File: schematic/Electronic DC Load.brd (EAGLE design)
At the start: 100 x 51.2 mm, 104 parts, among them J1 POWER_JACKPTH_LOCK, J2 AVR_SPI_PROG_3X2PTH, J3 FAN, J4 KF762-2, Q1 16MHz, Q2 IRFP250NV, Q3 600mA/40V, U1 AMS1117-5.0, U10 AD8629ARZ, U2 REF5050_D_8, U3 ATMEGA328P_TQFP, U4 MP1584EN, U5 LM35_LP_3, U6 AD7190BRUZ, U7 AD5541ARZ, U8 INA210AIDCKRG4, U9 PCF8574_DW_16

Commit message: Change debouncing filter network resistor to 1K
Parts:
- R12, R17, R19, R22, R24, R25, R27: value 10K -> 1K
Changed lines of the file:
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@@
 <attribute name="VALUE" x="38.0238" y="40.0304" size="1.27" layer="27"/>
 </element>
-<element name="R12" library="resistor" library_urn="urn:adsk.eagle:library:348" package="R0603" package3d_urn="urn:adsk.eagle:package:26057/1" value="10K" x="94.9452" y="10.2108" smashed="yes" rot="MR270">
+<element name="R12" library="resistor" library_urn="urn:adsk.eagle:library:348" package="R0603" package3d_urn="urn:adsk.eagle:package:26057/1" value="1K" x="94.9452" y="10.2108" smashed="yes" rot="MR270">
 <attribute name="NAME" x="94.1832" y="12.5222" size="0.6096" layer="26" rot="MR180"/>
 <attribute name="VALUE" x="96.8502" y="10.8458" size="1.27" layer="28" rot="MR270"/>
@@
 <attribute name="VALUE" x="40.4368" y="7.8486" size="1.27" layer="28" rot="MR270"/>
 </element>
-<element name="R19" library="resistor" library_urn="urn:adsk.eagle:library:348" package="R0603" package3d_urn="urn:adsk.eagle:package:26057/1" value="10K" x="41.7068" y="8.9916" smashed="yes" rot="MR0">
+<element name="R19" library="resistor" library_urn="urn:adsk.eagle:library:348" package="R0603" package3d_urn="urn:adsk.eagle:package:26057/1" value="1K" x="41.7068" y="8.9916" smashed="yes" rot="MR0">
 <attribute name="NAME" x="41.7068" y="10.2108" size="0.6096" layer="26" rot="MR0"/>
 <attribute name="VALUE" x="42.3418" y="7.0866" size="1.27" layer="28" rot="MR0"/>
@@
 <attribute name="VALUE" x="50.8508" y="7.8486" size="1.27" layer="28" rot="MR270"/>
 </element>
-<element name="R17" library="resistor" library_urn="urn:adsk.eagle:library:348" package="R0603" package3d_urn="urn:adsk.eagle:package:26057/1" value="10K" x="51.9938" y="8.9916" smashed="yes" rot="MR0">
+<element name="R17" library="resistor" library_urn="urn:adsk.eagle:library:348" package="R0603" package3d_urn="urn:adsk.eagle:package:26057/1" value="1K" x="51.9938" y="8.9916" smashed="yes" rot="MR0">
 <attribute name="NAME" x="51.943" y="10.3124" size="0.6096" layer="26" rot="MR0"/>
 <attribute name="VALUE" x="52.6288" y="7.0866" size="1.27" layer="28" rot="MR0"/>
@@
 <attribute name="VALUE" x="85.1662" y="8.8138" size="1.27" layer="28" rot="MR180"/>
 </element>
-<element name="R22" library="resistor" library_urn="urn:adsk.eagle:library:348" package="R0603" package3d_urn="urn:adsk.eagle:package:26057/1" value="10K" x="85.8012" y="4.6228" smashed="yes" rot="MR180">
+<element name="R22" library="resistor" library_urn="urn:adsk.eagle:library:348" package="R0603" package3d_urn="urn:adsk.eagle:package:26057/1" value="1K" x="85.8012" y="4.6228" smashed="yes" rot="MR180">
 <attribute name="VALUE" x="85.1662" y="6.5278" size="1.27" layer="28" rot="MR180"/>
 </element>
@@
 <attribute name="VALUE" x="85.1662" y="11.3538" size="1.27" layer="28" rot="MR180"/>
 </element>
-<element name="R24" library="resistor" library_urn="urn:adsk.eagle:library:348" package="R0603" package3d_urn="urn:adsk.eagle:package:26057/1" value="10K" x="85.8012" y="11.7348" smashed="yes" rot="MR180">
+<element name="R24" library="resistor" library_urn="urn:adsk.eagle:library:348" package="R0603" package3d_urn="urn:adsk.eagle:package:26057/1" value="1K" x="85.8012" y="11.7348" smashed="yes" rot="MR180">
 <attribute name="VALUE" x="85.1662" y="13.6398" size="1.27" layer="28" rot="MR180"/>
 </element>
@@
 <attribute name="VALUE" x="61.0108" y="7.8486" size="1.27" layer="28" rot="MR270"/>
 </element>
-<element name="R27" library="resistor" library_urn="urn:adsk.eagle:library:348" package="R0603" package3d_urn="urn:adsk.eagle:package:26057/1" value="10K" x="62.2808" y="8.9916" smashed="yes" rot="MR0">
+<element name="R27" library="resistor" library_urn="urn:adsk.eagle:library:348" package="R0603" package3d_urn="urn:adsk.eagle:package:26057/1" value="1K" x="62.2808" y="8.9916" smashed="yes" rot="MR0">
 <attribute name="NAME" x="62.1284" y="10.16" size="0.6096" layer="26" rot="MR0"/>
 <attribute name="VALUE" x="62.9158" y="7.0866" size="1.27" layer="28" rot="MR0"/>
@@
 <attribute name="VALUE" x="71.3486" y="7.7978" size="1.27" layer="28" rot="MR270"/>
 </element>
-<element name="R25" library="resistor" library_urn="urn:adsk.eagle:library:348" package="R0603" package3d_urn="urn:adsk.eagle:package:26057/1" value="10K" x="72.5678" y="8.9916" smashed="yes" rot="MR0">
+<element name="R25" library="resistor" library_urn="urn:adsk.eagle:library:348" package="R0603" package3d_urn="urn:adsk.eagle:package:26057/1" value="1K" x="72.5678" y="8.9916" smashed="yes" rot="MR0">
 <attribute name="NAME" x="72.4408" y="10.16" size="0.6096" layer="26" rot="MR0"/>
 <attribute name="VALUE" x="73.2028" y="7.0866" size="1.27" layer="28" rot="MR0"/>

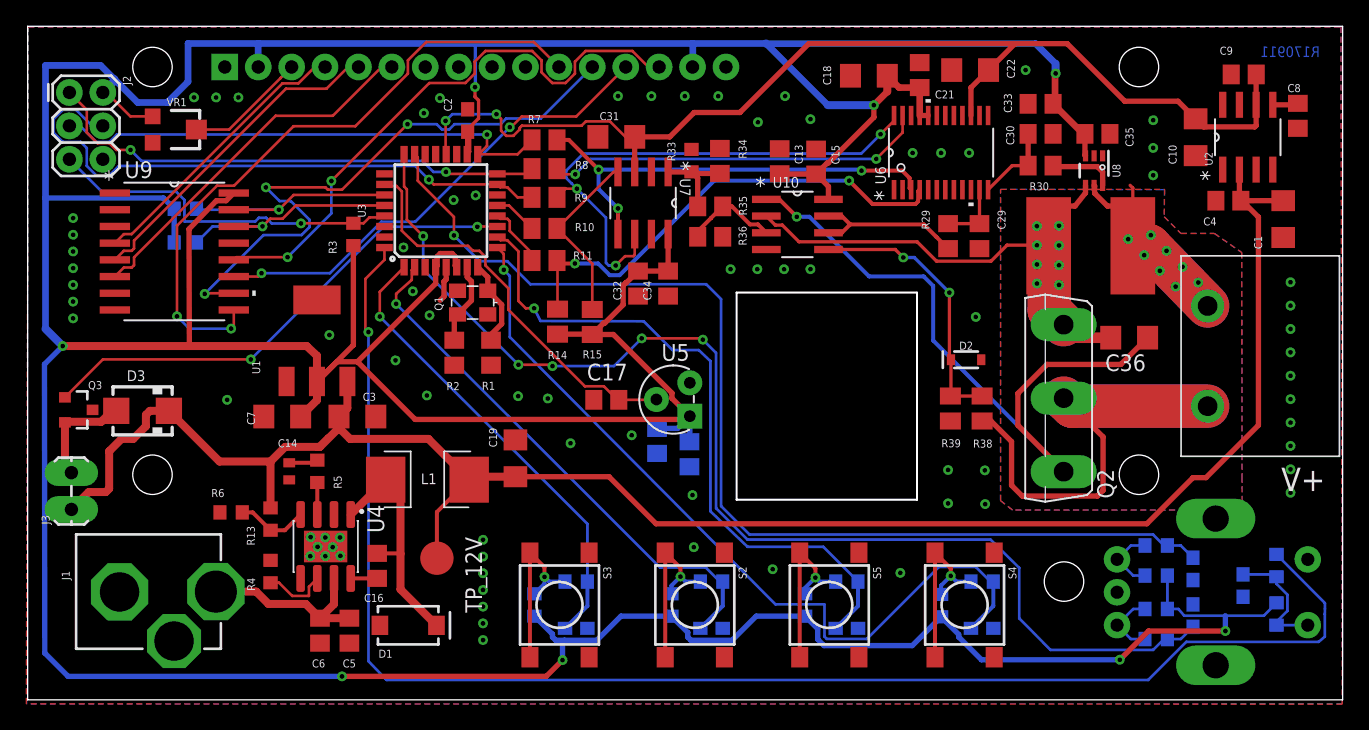
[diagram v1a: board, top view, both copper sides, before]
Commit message: Fix lableling errors
Fix a few errors in the labeling of resistors and capacitors
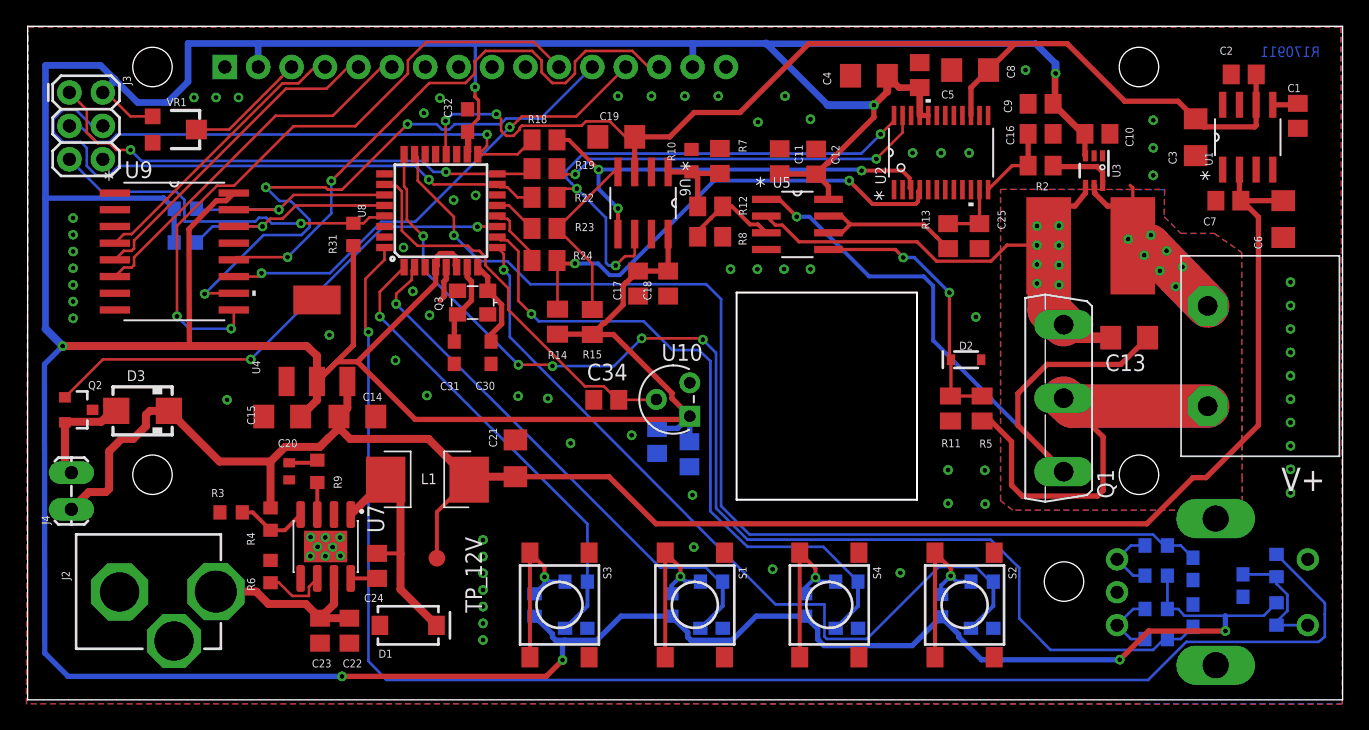
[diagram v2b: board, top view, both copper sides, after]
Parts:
- removed R38: 39K 0.1%, resistor:M0805
- removed R39: 1K 0.1%, resistor:M0805
- added C37: 1uF, resistor:C0805
- added C38: 100nF, resistor:C0805
- C1, C22: value 10uF -> 1uF; device resistor:C1206 -> resistor:C0805
- C10: value 47uF -> 100nF; device resistor:C1206 -> resistor:C0805
- C13, C8: value 1uF -> 10uF; device resistor:C0805 -> resistor:C1206
- C14: value 150pF -> 10uF; device resistor:C0402 -> resistor:C1206
- C15: value 100nF -> 22uF; device resistor:C0805 -> resistor:C1206
- C16, C34: value 100nF -> 1uF
- C18: value 10uF -> 100nF; device resistor:C1206 -> resistor:C0805
- C19: value 47uF -> 10uF
- C2, C25: value 100nF -> 1uF; device resistor:C0603 -> resistor:C0805
- C20: value 100nF -> 150pF; device resistor:C0603 -> resistor:C0402
- C21: value 100nF -> 47uF; device resistor:C0805 -> resistor:C1206
- C23, C24: device resistor:C0603 -> resistor:C0805
- C29, C32, C33: value 1uF -> 100nF; device resistor:C0805 -> resistor:C0603
- C3: value 10uF -> 47uF
- C30: value 1uF -> 8.2pF; device resistor:C0805 -> resistor:C0603
- C31: value 10uF -> 8.2pF; device resistor:C1206 -> resistor:C0603
- C35: device resistor:C0805 -> resistor:C0603
- C36: value 10uF -> 100nF; device resistor:C1206 -> resistor:C0603
- C4, C6: value 100nF -> 10uF; device resistor:C0805 -> resistor:C1206
- C5: value 1uF -> 100nF
- C7: value 22uF -> 100nF; device resistor:C1206 -> resistor:C0805
- J1: value POWER_JACKPTH_LOCK -> KF762-2; device SparkFun-Connectors:POWER_JACK_PTH_LOCK -> 0_discrete:KF762-2
- J2: value AVR_SPI_PROG_3X2PTH -> POWER_JACKPTH_LOCK; device SparkFun-Connectors:2X3 -> SparkFun-Connectors:POWER_JACK_PTH_LOCK
- J3: value FAN -> AVR_SPI_PROG_3X2PTH; device SparkFun-Connectors:1X02_LOCK_LONGPADS -> SparkFun-Connectors:2X3
- J4: value KF762-2 -> FAN; device 0_discrete:KF762-2 -> SparkFun-Connectors:1X02_LOCK_LONGPADS
- Q1: value 16MHz -> IRFP250NV; device crystal-geyer_V1_0:3.2X2.5_KX-7 -> 0_discrete:TO247BV
- Q2: value IRFP250NV -> 600mA/40V; device 0_discrete:TO247BV -> SparkFun-DiscreteSemi:SOT23-3
- Q3: value 600mA/40V -> 16MHz; device SparkFun-DiscreteSemi:SOT23-3 -> crystal-geyer_V1_0:3.2X2.5_KX-7
- R1: value 10pF -> .005; device resistor:R0805 -> 0_sup:2728
- R10: value 100 -> 10K; device resistor:M0805 -> resistor:R0603
- R11: value 100 -> 1K 0.1%
- R12: value 1K -> 39K 0.1%; device resistor:R0603 -> resistor:R0805
- R13: value 150K -> 1K; device resistor:R0603 -> resistor:R0805
- R17, R25, R27: value 1K -> 10K
- R18, R23: value 10K -> 100; device resistor:R0603 -> resistor:M0805
- R19, R22, R24: value 1K -> 100; device resistor:R0603 -> resistor:M0805
- R2: value 10pF -> 1K
- R29, R30: value 1K -> 10K; device resistor:R0805 -> resistor:R0603
- R3: value 10K -> 10.5K
- R34: value 1uF -> 10K; device resistor:R0805 -> resistor:R0603
- R35: value 39K 0.1% -> 10K; device resistor:R0805 -> resistor:R0603
- R36: value 10K 0.1% -> 10K; device resistor:R0805 -> resistor:R0603
- R37: value .005 -> 10K; device 0_sup:2728 -> resistor:R0603
- R4: value 120K -> 150K
- R5: value 500K -> 9K9 0.1%; device resistor:R0603 -> resistor:M0805
- R6: value 10.5K -> 120K
- R7: value 100 -> 1uF; device resistor:M0805 -> resistor:R0805
- R8: value 100 -> 10K 0.1%; device resistor:M0805 -> resistor:R0805
- R9: value 100 -> 510K; device resistor:M0805 -> resistor:R0603
- S1: value ENCODER_SWITCH_EC11 -> SWITCH_6X6; device 0_discrete:ROTARY_ENCODER_EC11 -> 0_discrete:SWITCH_SMD_6MM
- S5: value SWITCH_6X6 -> ENCODER_SWITCH_EC11; device 0_discrete:SWITCH_SMD_6MM -> 0_discrete:ROTARY_ENCODER_EC11
- TP_12V: value TPB2,54 -> TPB1,27; device testpad:B2,54 -> testpad:B1,27
- U1: value AMS1117-5.0 -> REF5050_D_8; device AMS1117-5.0:SOT223 -> 0_texas-instrument:D8
- U10: value AD8629ARZ -> LM35_LP_3; device 0_analog-devices:R_8 -> 0_texas-instrument:Z03A
- U2: value REF5050_D_8 -> AD7190BRUZ; device 0_texas-instrument:D8 -> 0_analog-devices:RU_24
- U3: value ATMEGA328P_TQFP -> INA210AIDCKRG4; device SparkFun-IC-Microcontroller:TQFP32-08 -> 0_texas-instrument:DCK0006A_N
- U4: value MP1584EN -> AMS1117-5.0; device MP1584EN:SOIC9P127_490X600X170L84X42T330X241N -> AMS1117-5.0:SOT223
- U5: value LM35_LP_3 -> AD8629ARZ; device 0_texas-instrument:Z03A -> 0_analog-devices:R_8
- U6: value AD7190BRUZ -> AD5541ARZ; device 0_analog-devices:RU_24 -> 0_analog-devices:R_8
- U7: value AD5541ARZ -> MP1584EN; device 0_analog-devices:R_8 -> MP1584EN:SOIC9P127_490X600X170L84X42T330X241N
- U8: value INA210AIDCKRG4 -> ATMEGA328P_TQFP; device 0_texas-instrument:DCK0006A_N -> SparkFun-IC-Microcontroller:TQFP32-08
- moved J1 91.1 mm to (89.7, 26.1)
- moved J4 87.2 mm to (3.33, 14.6), turned to 90 degrees
- moved R32 86.5 mm to (94.9, 10.2), turned to 270 degrees
- moved C6 79.6 mm to (95.5, 36.6), turned to 90 degrees
- moved C7 73.8 mm to (91.3, 37.9)
- moved C20 73.0 mm to (19.9, 17.4), flipped to the top, turned to 270 degrees
- moved U1 72.4 mm to (92.8, 42.8)
- moved Q2 72.0 mm to (3.84, 22.0), turned to 270 degrees
- moved C3 67.2 mm to (88.8, 42.8), turned to 90 degrees
- moved R30 65.3 mm to (12.0, 34.8), flipped to the bottom, turned to 0 degrees
- moved C22 63.6 mm to (24.5, 5.26), turned to 270 degrees
- moved C5 60.5 mm to (67.8, 47.5)
- moved C16 60.2 mm to (77.0, 43.0), turned to 180 degrees
- moved C2 59.1 mm to (92.5, 47.5), turned to 0 degrees
- moved R29 58.0 mm to (12.0, 37.3), flipped to the bottom, turned to 0 degrees
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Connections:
- net !ADC_CS: now also R24.2, U2.4; no longer R11.2, U6.4
- net !DAC_CS: now also R23.2, U6.4; no longer R10.2, U7.4
- net +12V: now also C14.2, C21.1, C6.2, C7.2, J4.1, R4.2, U1.2, U4.3; no longer C1.2, C19.1, C3.2, C4.2, J3.1, R13.2, U1.3, U2.2
- net +5V: now also C10.2, C17.2, C37.2, C38.2, C4.2, C5.2, C9.2, J3.2, R27.2, R29.2, R30.2, R31.1, R34.2, R36.2, R37.2, U10.1, U2.20, U2.21, U3.3, U4.2, U5.8, U6.8, U8.18, U8.4, U8.6; no longer C13.2, C2.2, C21.2, C33.2, C34.2, C35.2, C7.2, J2.2, R16.2, R18.2, R23.2, R26.2, R3.1, R31.2, R32.2, U1.2, U10.8, U3.18, U3.4, U3.6, U5.1, U6.20, U6.21, U7.8, U8.3
- net C_SENSE: now also C13.2, Q1.S, R1.2, U3.4, U5.2; no longer C36.2, Q2.S, R37.2, U10.2, U8.4
- net FAN_SW: now also Q2.1, U8.11; no longer Q3.1, U3.11
- net GND: now also C14.1, C16.1, C19.1, C20.2, C21.2, C22.2, C25.1, C29.2, C33.2, C36.2, C37.1, C38.1, C5.1, C6.1, J1.1, J2.GND, J2.GNDBREAK, J3.6, Q2.3, R10.2, R11.2, R3.2, R7.1, R8.2, S1.B1, S1.B2, S5.C, S5.D, U1.4, U10.3, U2.10, U2.16, U2.18, U2.19, U3.1, U3.2, U4.1, U5.4, U6.2, U6.7, U7.5, U7.9, U8.21, U8.3; no longer C13.1, C14.2, C19.2, C20.1, C21.1, C22.1, C24.2, C25.2, C29.1, C33.1, C5.2, C6.2, J1.GND, J1.GNDBREAK, J2.6, J4.1, Q3.3, R2.1, R33.2, R34.1, R36.2, R37.1, R39.2, R4.2, S1.C, S1.D, S5.B1, S5.B2, U1.1, U10.4, U2.4, U3.21, U3.3, U4.5, U4.9, U5.3, U6.10, U6.16, U6.18, U6.19, U7.2, U7.7, U8.1, U8.2
- net MISO: now also R19.2, U2.23; no longer R8.2, U6.23
- net MOSI: now also R22.2, U2.24, U6.6; no longer R9.2, U6.24, U7.6
- net N$1: now also R29.1, U8.27; no longer R31.1, U3.27
- net N$10: now also C1.2, U1.5; no longer C8.2, U2.5
- net N$11: now also C31.2, Q3.3, U8.7; no longer Q1.3, R2.2, U3.7
- net N$12: now also C30.2, Q3.1, U8.8; no longer Q1.1, R1.2, U3.8
- net N$14: now also J1.2, Q1.D, R5.1; no longer J4.2, Q2.D, R38.1
- net N$15: now also C34.2, U10.2, U8.26; no longer C17.2, U3.26, U5.2
- net N$16: now also C25.2, R13.2, U2.11; no longer C29.2, R29.2, U6.11
- net N$17: now also R6.1, U7.6; no longer R4.1, U4.6
- net N$18: now also R2.1, U3.6; no longer R30.1, U8.6
- net N$19: now also C24.1, U7.8; no longer C16.1, U4.8
- net N$2: now also R30.1, U8.28; no longer R32.1, U3.28
- net N$20: now also C22.1, C23.1, J2.PWR, U7.7; no longer C5.1, C6.1, J1.PWR, U4.7
- net N$21: now also C24.2, U7.1; no longer C16.2, U4.1
- net N$22: now also R3.1, R4.1, U7.4; no longer R13.1, R6.1, U4.4
- net N$23: now also R9.1, U7.3; no longer R5.1, U4.3
- net N$24: now also C16.2, R2.2, U2.12; no longer C30.2, R30.2, U6.12
- net N$25: now also C20.1, R9.2; no longer C14.1, R5.2
- net N$26: now also R10.1, R12.1, R7.2, U6.1; no longer R33.1, R34.2, R35.1, U7.1
- net N$27: now also R13.1, U5.6, U5.7; no longer R29.1, U10.6, U10.7
- net N$28: now also J4.2, Q2.2; no longer J3.2, Q3.2
- net N$29: now also R35.1, R36.1, S5.B; no longer R21.1, R22.1, S1.B
- net N$30: now also J3.3, R18.1, U8.17; no longer J2.3, R7.1, U3.17
- net N$31: now also J3.1, R19.1, U8.16; no longer J2.1, R8.1, U3.16
- net N$32: now also J3.4, R22.1, U8.15; no longer J2.4, R9.1, U3.15
- net N$34: now also R23.1, U8.13; no longer R10.1, U3.13
- net N$35: now also R24.1, U8.12; no longer R11.1, U3.12
- net N$36: now also C13.1, Q1.G, U5.1; no longer C36.1, Q2.G, U10.1
- net N$37: now also R11.1, R5.2, U5.5; no longer R38.2, R39.1, U10.5
- net N$38: now also R33.1, R37.1, S5.A; no longer R23.1, R24.1, S1.A
- net N$39: now also R12.2, R8.1, U5.3; no longer R35.2, R36.1, U10.3
- net N$40: now also R16.2, R20.1, S1.A1, S1.A2; no longer R17.2, R18.1, S2.A1, S2.A2
- net N$41: now also R25.2, R27.1; no longer R19.2, R20.1
- net N$42: now also C35.2, R32.2, R34.1, S5.E; no longer C20.2, R12.2, R16.1, S1.E
- net N$43: now also C26.1, R16.1, U8.2; no longer C23.1, R17.1, U3.2
- net N$44: now also R32.1, U8.32; no longer R12.1, U3.32
- net N$46: now also C28.1, R25.1, U8.1; no longer C24.1, R19.1, U3.1
- net N$48: now also R26.2, S4.A1, S4.A2; no longer R27.2, S5.A1, S5.A2
- net N$51: now also R17.2, R21.1, S2.A1, S2.A2; no longer R25.2, R26.1, S4.A1, S4.A2
- net N$52: now also C27.1, R17.1, U8.9; no longer C26.1, R25.1, U3.9
- net N$55: now also C29.1, R26.1, U8.10; no longer C27.1, R27.1, U3.10
- net RESET: now also J3.5, R31.2, U8.29; no longer J2.5, R3.2, U3.29
- net ROTARY_A: now also C33.1, R33.2, U8.23; no longer C28.1, R24.2, U3.23
- net ROTARY_B: now also C36.1, R35.2, U8.24; no longer C25.1, R22.2, U3.24
- net SCLK: now also R18.2, U2.3, U6.5; no longer R7.2, U6.3, U7.5
- net VREF: now also C19.2, C2.2, C3.2, C8.2, U1.6, U2.15, U6.3, U8.20; no longer C10.2, C22.2, C31.2, C9.2, U2.6, U3.20, U6.15, U7.3

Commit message: Remove the ground bridge for Rsense
I made the ground bridge not sure if it's needed.
And obviously, it doesn't. And removing it will tremendously increase the accuracy of INA213!!!
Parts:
- removed R10: 10K, resistor:R0603
- D2: device 0_discrete:SOD-323 -> 0_discrete:LL-34
- R7: device resistor:R0805 -> resistor:C0805
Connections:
- net GND: no longer R10.2
- net N$26: no longer R10.1
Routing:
- net GND: track 29.3 -> 24.7 mm
- net N$26: track 6.82 -> 8.58 mm
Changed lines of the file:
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@@
 <attribute name="VALUE" x="34.9758" y="25.7556" size="1.27" layer="27" rot="R90"/>
 </element>
-<element name="R7" library="resistor" library_urn="urn:adsk.eagle:library:348" package="R0805" package3d_urn="urn:adsk.eagle:package:26059/1" value="1uF" x="52.6288" y="40.9702" smashed="yes" rot="R270">
+<element name="R7" library="resistor" library_urn="urn:adsk.eagle:library:348" package="C0805" package3d_urn="urn:adsk.eagle:package:26137/1" value="1uF" x="52.6288" y="40.9702" smashed="yes" rot="R270">
 <attribute name="NAME" x="54.0512" y="42.6212" size="0.6096" layer="25" rot="R270"/>
 <attribute name="VALUE" x="50.0888" y="41.6052" size="1.27" layer="27" rot="R270"/>
@@
 <attribute name="VALUE" x="28.9306" y="4.0132" size="0.6096" layer="27" font="vector" ratio="20" align="top-center"/>
 </element>
-<element name="D2" library="0_discrete" package="SOD-323" value="5.1V" x="71.3486" y="25.8572" smashed="yes">
+<element name="D2" library="0_discrete" package="LL-34" value="5.1V" x="71.3486" y="25.8572" smashed="yes">
 <attribute name="NAME" x="71.3486" y="26.6192" size="0.6096" layer="25" font="vector" ratio="20" align="bottom-center"/>
 <attribute name="VALUE" x="71.3486" y="25.0952" size="0.6096" layer="27" font="vector" ratio="20" align="top-center"/>
@@
 <attribute name="NAME" x="13.4874" y="32.9946" size="0.6096" layer="26" rot="MR0"/>
 <attribute name="VALUE" x="12.6238" y="32.8676" size="1.27" layer="28" rot="MR0"/>
-</element>
-<element name="R10" library="resistor" library_urn="urn:adsk.eagle:library:348" package="R0603" package3d_urn="urn:adsk.eagle:package:26057/1" value="10K" x="50.4698" y="40.9956" smashed="yes" rot="R90">
-<attribute name="NAME" x="49.2506" y="40.9448" size="0.6096" layer="25" rot="R90"/>
-<attribute name="VALUE" x="52.3748" y="40.3606" size="1.27" layer="27" rot="R90"/>
 </element>
 <element name="R12" library="resistor" library_urn="urn:adsk.eagle:library:348" package="R0805" package3d_urn="urn:adsk.eagle:package:26059/1" value="39K 0.1%" x="51.8922" y="37.5158" smashed="yes">
@@
 <contactref element="C34" pad="1"/>
 <contactref element="C25" pad="1"/>
-<contactref element="R10" pad="2"/>
-<contactref element="R7" pad="1"/>
 <contactref element="R8" pad="2"/>
 <contactref element="Q2" pad="3"/>
@@
 <via x="22.6314" y="10.922" extent="1-16" drill="0.35"/>
 <via x="23.7744" y="10.9474" extent="1-16" drill="0.35"/>
-<wire x1="84.0228" y1="34.5186" x2="84.0228" y2="38.9132" width="0.254" layer="1"/>
-<wire x1="84.0228" y1="38.9132" x2="83.82" y2="39.116" width="0.254" layer="1"/>
 <wire x1="31.8198" y1="32.893" x2="31.8198" y2="31.9764125" width="0.4064" layer="1"/>
 <wire x1="31.8198" y1="31.9764125" x2="31.6518" y2="31.8084125" width="0.4064" layer="1"/>
@@
 <via x="28.575" y="34.3916" extent="1-16" drill="0.35"/>
 <contactref element="C32" pad="1"/>
+<contactref element="R7" pad="1"/>
+<wire x1="81.0768" y1="39.1086" x2="81.0768" y2="41.3586" width="0" layer="19" extent="1-1"/>
 </signal>
 <signal name="N$11">
@@
 </signal>
 <signal name="N$26">
-<contactref element="R10" pad="1"/>
 <contactref element="R7" pad="2"/>
 <contactref element="U6" pad="1"/>
 <contactref element="R12" pad="1"/>
-<wire x1="50.4562" y1="40.132" x2="50.4698" y2="40.1456" width="0.4064" layer="1"/>
-<wire x1="50.4562" y1="40.132" x2="48.6918" y2="40.132" width="0.4064" layer="1"/>
-<wire x1="50.4698" y1="40.1456" x2="50.5952" y2="40.0202" width="0.4064" layer="1"/>
-<wire x1="50.5952" y1="40.0202" x2="52.6288" y2="40.0202" width="0.4064" layer="1"/>
-<wire x1="50.4698" y1="40.1456" x2="50.9422" y2="39.6732" width="0.4064" layer="1"/>
-<wire x1="50.9422" y1="39.6732" x2="50.9422" y2="37.5158" width="0.4064" layer="1"/>
+<wire x1="50.9422" y1="39.5834" x2="50.9422" y2="37.5158" width="0.3048" layer="1"/>
+<wire x1="50.9422" y1="39.5834" x2="50.3936" y2="40.132" width="0.3048" layer="1"/>
+<wire x1="50.3936" y1="40.132" x2="48.6918" y2="40.132" width="0.3048" layer="1"/>
+<wire x1="50.9422" y1="37.5158" x2="50.9422" y2="39.563" width="0.3048" layer="1"/>
+<wire x1="50.9422" y1="39.563" x2="51.5366" y2="40.1574" width="0.3048" layer="1"/>
+<wire x1="51.5366" y1="40.1574" x2="52.4916" y2="40.1574" width="0.3048" layer="1"/>
+<wire x1="52.4916" y1="40.1574" x2="52.6288" y2="40.0202" width="0.3048" layer="1"/>
 </signal>
 <signal name="N$30">
@@
 <wire x1="72.5678" y1="23.0988" x2="70.1548" y2="23.0988" width="0.254" layer="1"/>
 <wire x1="70.1548" y1="23.0988" x2="70.1986" y2="23.1426" width="0.254" layer="1"/>
-<wire x1="70.1986" y1="23.1426" x2="70.1986" y2="25.8572" width="0.254" layer="1"/>
-<wire x1="70.1986" y1="25.8572" x2="70.0786" y2="25.9772" width="0.254" layer="1"/>
+<wire x1="70.1986" y1="23.1426" x2="69.8486" y2="25.8572" width="0.254" layer="1"/>
+<wire x1="69.8486" y1="25.8572" x2="70.0786" y2="25.9772" width="0.254" layer="1"/>
 <wire x1="70.0786" y1="25.9772" x2="70.0786" y2="30.9626" width="0.254" layer="1"/>
 <via x="70.0786" y="30.9626" extent="1-16" drill="0.35"/>
